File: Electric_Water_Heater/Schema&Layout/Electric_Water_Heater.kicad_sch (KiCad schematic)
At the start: 26 parts, among them J1 Barrel_Jack_Switch, SW1 SW_Push, U1 ATmega32A-P, U2 L7805, U3 7447, U4 ELD-426SYGWA, U5 ST24C08, Y1 16MHz

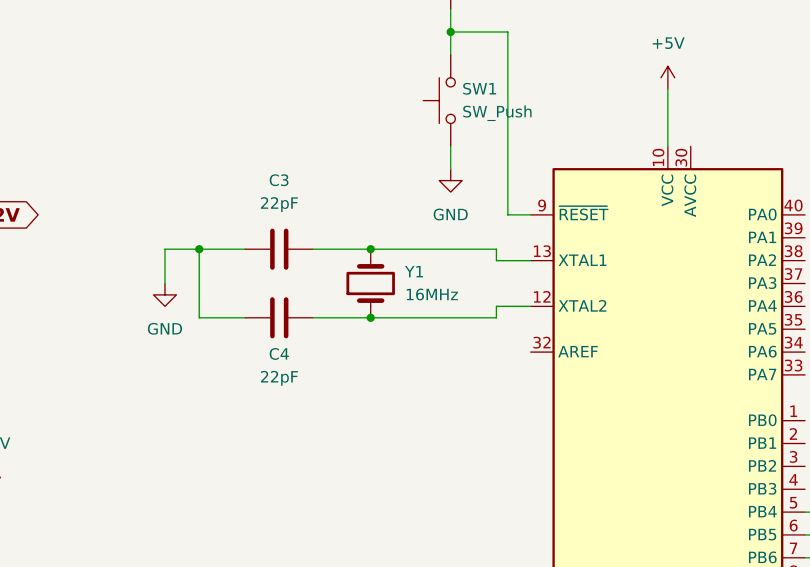
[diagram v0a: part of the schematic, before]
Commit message: Integrate I2C External EEPROM With Seven Segment
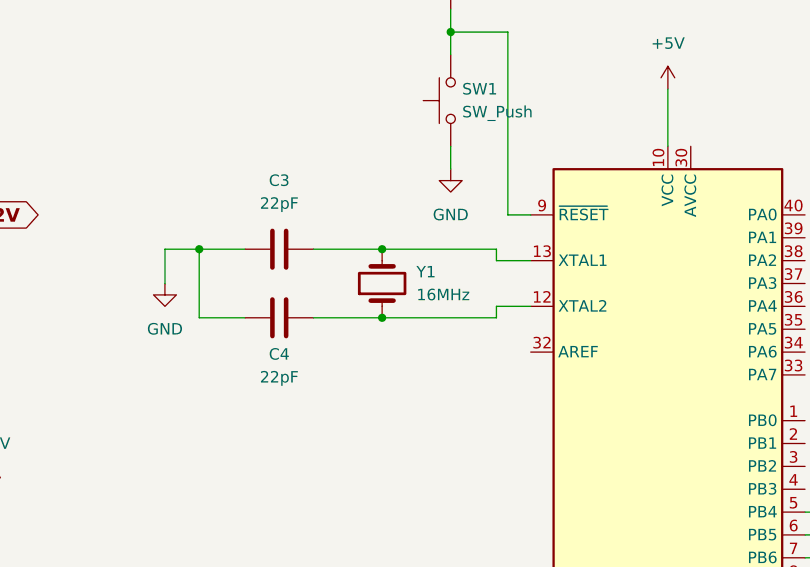
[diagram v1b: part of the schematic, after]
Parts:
- Y1: footprint (none) -> Crystal:Crystal_HC49-4H_Vertical
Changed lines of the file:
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@@
 	)
 	(junction
-		(at 119.38 72.39)
-		(diameter 0)
-		(color 0 0 0 0)
-	)
-	(junction
 		(at 39.37 66.04)
 		(diameter 0)
@@
 	)
 	(junction
-		(at 119.38 64.77)
+		(at 120.65 64.77)
 		(diameter 0)
 		(color 0 0 0 0)
@@
 	)
 	(junction
+		(at 120.65 72.39)
+		(diameter 0)
+		(color 0 0 0 0)
+	)
+	(junction
 		(at 66.04 91.44)
 		(diameter 0)
@@
 	(wire
 		(pts
-			(xy 119.38 72.39) (xy 133.35 72.39)
+			(xy 113.03 72.39) (xy 120.65 72.39)
 		)
 		(stroke
@@
 	(wire
 		(pts
-			(xy 113.03 64.77) (xy 119.38 64.77)
-		)
-		(stroke
-			(width 0)
-			(type default)
-		)
-	)
-	(wire
-		(pts
 			(xy 198.12 121.92) (xy 208.28 121.92)
 		)
@@
 	(wire
 		(pts
+			(xy 120.65 72.39) (xy 133.35 72.39)
+		)
+		(stroke
+			(width 0)
+			(type default)
+		)
+	)
+	(wire
+		(pts
 			(xy 232.41 45.72) (xy 229.87 45.72)
 		)
@@
 	(wire
 		(pts
-			(xy 113.03 72.39) (xy 119.38 72.39)
-		)
-		(stroke
-			(width 0)
-			(type default)
-		)
-	)
-	(wire
-		(pts
 			(xy 66.04 93.98) (xy 66.04 91.44)
 		)
@@
 	(wire
 		(pts
-			(xy 133.35 64.77) (xy 119.38 64.77)
+			(xy 113.03 64.77) (xy 120.65 64.77)
 		)
 		(stroke
@@
 	(wire
 		(pts
+			(xy 120.65 64.77) (xy 133.35 64.77)
+		)
+		(stroke
+			(width 0)
+			(type default)
+		)
+	)
+	(wire
+		(pts
 			(xy 39.37 66.04) (xy 39.37 72.39)
 		)
@@
 	)
 	(symbol
+		(lib_id "Device:Crystal")
+		(at 120.65 68.58 90)
+		(unit 1)
+		(exclude_from_sim no)
+		(in_bom yes)
+		(on_board yes)
+		(dnp no)
+		(fields_autoplaced yes)
+		(property "Reference" "Y1"
+			(at 124.46 67.3099 90)
+			(effects
+				(font
+					(size 1.27 1.27)
+				)
+				(justify right)
+			)
+		)
+		(property "Value" "16MHz"
+			(at 124.46 69.8499 90)
+			(effects
+				(font
+					(size 1.27 1.27)
+				)
+				(justify right)
+			)
+		)
+		(property "Footprint" "Crystal:Crystal_HC49-4H_Vertical"
+			(at 120.65 68.58 0)
+			(effects
+				(font
+					(size 1.27 1.27)
+				)
+				(hide yes)
+			)
+		)
+		(property "Datasheet" "~"
+			(at 120.65 68.58 0)
+			(effects
+				(font
+					(size 1.27 1.27)
+				)
+				(hide yes)
+			)
+		)
+		(property "Description" "Two pin crystal"
+			(at 120.65 68.58 0)
+			(effects
+				(font
+					(size 1.27 1.27)
+				)
+				(hide yes)
+			)
+		)
+		(pin "1"
+		)
+		(pin "2"
+		)
+		(instances
+			(project ""
+				(path "/bb2186c6-1d5c-41ff-b914-7b8e78ba1812"
+					(reference "Y1")
+					(unit 1)
+				)
+			)
+		)
+	)
+	(symbol
 		(lib_id "Device:R")
 		(at 236.22 55.88 90)
@@
 					(unit 1)
 				)
-			)
-		)
-	)
-	(symbol
-		(lib_id "Device:Crystal")
-		(at 119.38 68.58 90)
-		(unit 1)
-		(exclude_from_sim no)
-		(in_bom yes)
-		(on_board yes)
-		(dnp no)
-		(fields_autoplaced yes)
-		(property "Reference" "Y1"
-			(at 123.19 67.3099 90)
-			(effects
-				(font
-					(size 1.27 1.27)
-				)
-				(justify right)
-			)
-		)
-		(property "Value" "16MHz"
-			(at 123.19 69.8499 90)
-			(effects
-				(font
-					(size 1.27 1.27)
-				)
-				(justify right)
-			)
-		)
-		(property "Footprint" ""
-			(at 119.38 68.58 0)
-			(effects
-				(font
-					(size 1.27 1.27)
-				)
-				(hide yes)
-			)
-		)
-		(property "Datasheet" "~"
-			(at 119.38 68.58 0)
-			(effects
-				(font
-					(size 1.27 1.27)
-				)
-				(hide yes)
-			)
-		)
-		(property "Description" "Two pin crystal"
-			(at 119.38 68.58 0)
-			(effects
-				(font
-					(size 1.27 1.27)
-				)
-				(hide yes)
-			)
-		)
-		(pin "1"
-		)
-		(pin "2"
-		)
-		(instances
-			(project ""
-				(path "/bb2186c6-1d5c-41ff-b914-7b8e78ba1812"
-					(reference "Y1")
-					(unit 1)
-				)
